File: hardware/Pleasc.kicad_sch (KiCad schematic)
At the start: 96 parts, among them J1 2601-1104, J3 ESQ-110-14-G-D, J4 2601-1104, J5 XT30PW-M, Q1 AO3400A, Q10 AO3400A, Q11 AO3400A, Q12 AO3400A, Q13 AO3400A, Q14 AO3400A, Q2 AO3400A, Q3 AO3400A, Q4 AO3400A, Q5 AO3400A, Q6 AO3400A, Q7 AO3400A, Q8 AO3400A, Q9 AO3400A, U1 STM32F072C8Tx, U10 LTV-817, U11 LTV-817, U12 LTV-817, U13 LTV-817, U18 LTV-817, U2 TLV70433DBVT, U3 LTV-817, U4 TJA1051T-3, U7 LTV-817, U8 LTV-817, U9 LTV-817

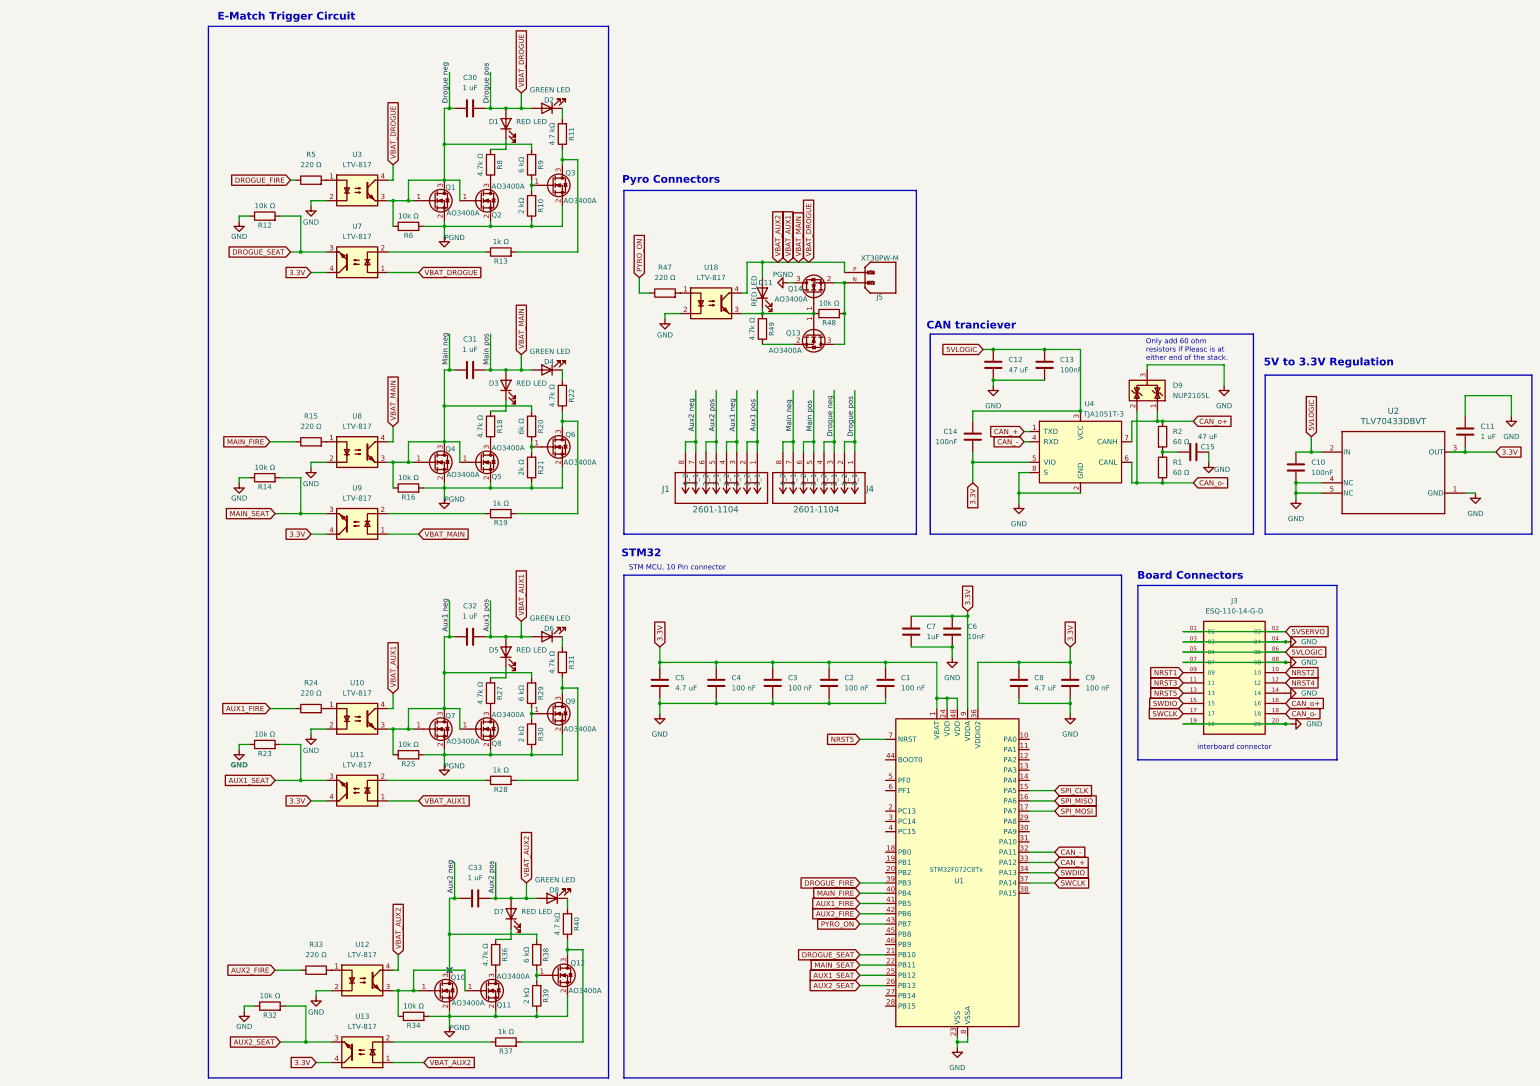
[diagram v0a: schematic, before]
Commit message: Schematic complete, components layed out on the PCB
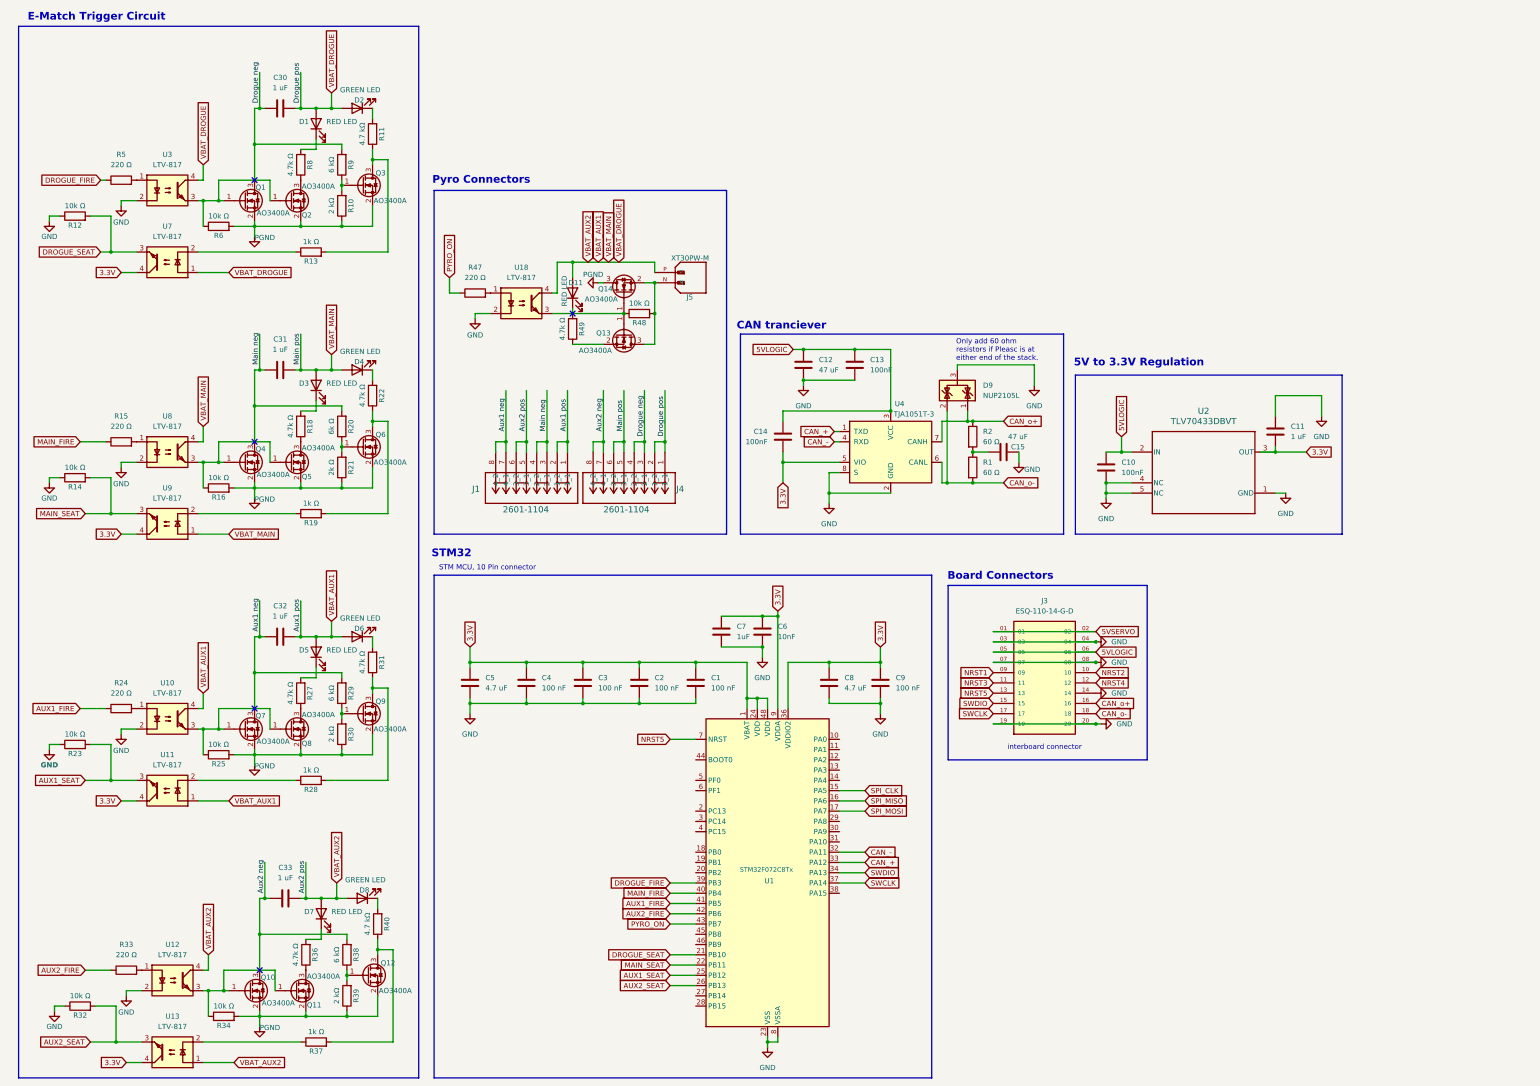
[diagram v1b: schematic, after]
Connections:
- net Aux1 neg: now also J1.7 (4_1), J1.8 (4_2); no longer J1.3 (2_1), J1.4 (2_2), Q7.1 (G), Q8.1 (G), R25.1, U10.3
- net Aux2 neg: now also J4.7 (4_1), J4.8 (4_2); no longer J1.7 (4_1), J1.8 (4_2), Q10.1 (G), Q11.1 (G), R34.1, U12.3
- net Drogue neg: no longer Q1.1 (G), Q2.1 (G), R6.1, U3.3
- net Main neg: now also J1.3 (2_1), J1.4 (2_2); no longer J4.7 (4_1), J4.8 (4_2), Q4.1 (G), Q5.1 (G), R16.1, U8.3
- net at Q13.1 (G), Q14.1 (G), R48.1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: no longer D11.1 (K), R49.2
- new net: Q10.1 (G), Q11.1 (G), R34.1, U12.3
- new net: Q1.1 (G), Q2.1 (G), R6.1, U3.3
- new net: Q4.1 (G), Q5.1 (G), R16.1, U8.3
- new net: D11.1 (K), R49.2
- new net: Q7.1 (G), Q8.1 (G), R25.1, U10.3
- no-connect marks 1 -> 5
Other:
- moved on the sheet: C1, C10, C11, C12, C13, C14, C15, C2, C3, C30, C31, C32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

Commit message: All 4 Pyros circuits routed
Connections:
- net Aux2 neg: now also J4.3 (2_1), J4.4 (2_2); no longer J4.7 (4_1), J4.8 (4_2)
- net Drogue neg: now also J4.7 (4_1), J4.8 (4_2); no longer J4.3 (2_1), J4.4 (2_2)
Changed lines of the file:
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@@
 	)
 	(label "Drogue neg"
-		(at 170.18 121.92 90)
+		(at 160.02 121.92 90)
 		(effects
 			(font
@@
 	)
 	(label "Aux2 neg"
-		(at 160.02 120.65 90)
+		(at 170.18 120.65 90)
 		(effects
 			(font

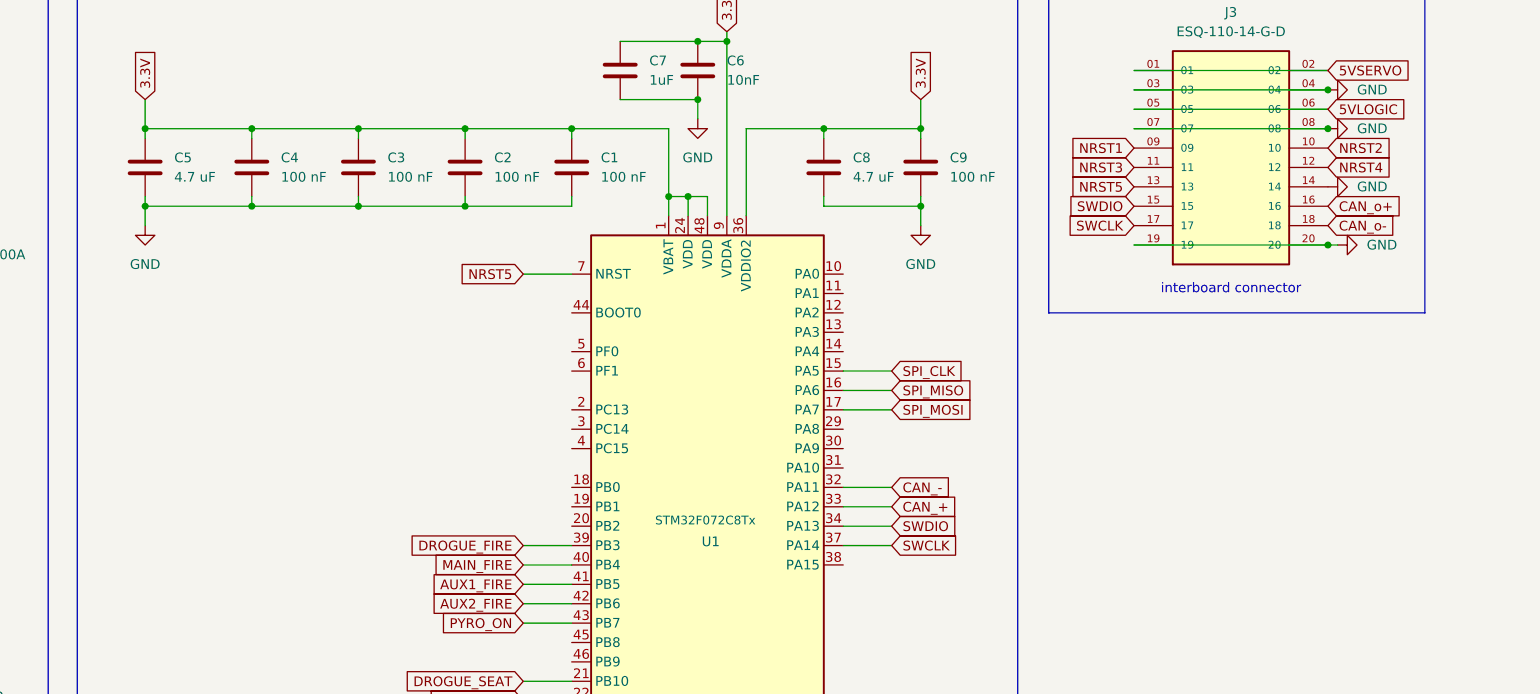
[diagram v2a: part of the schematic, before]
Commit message: added can crystal
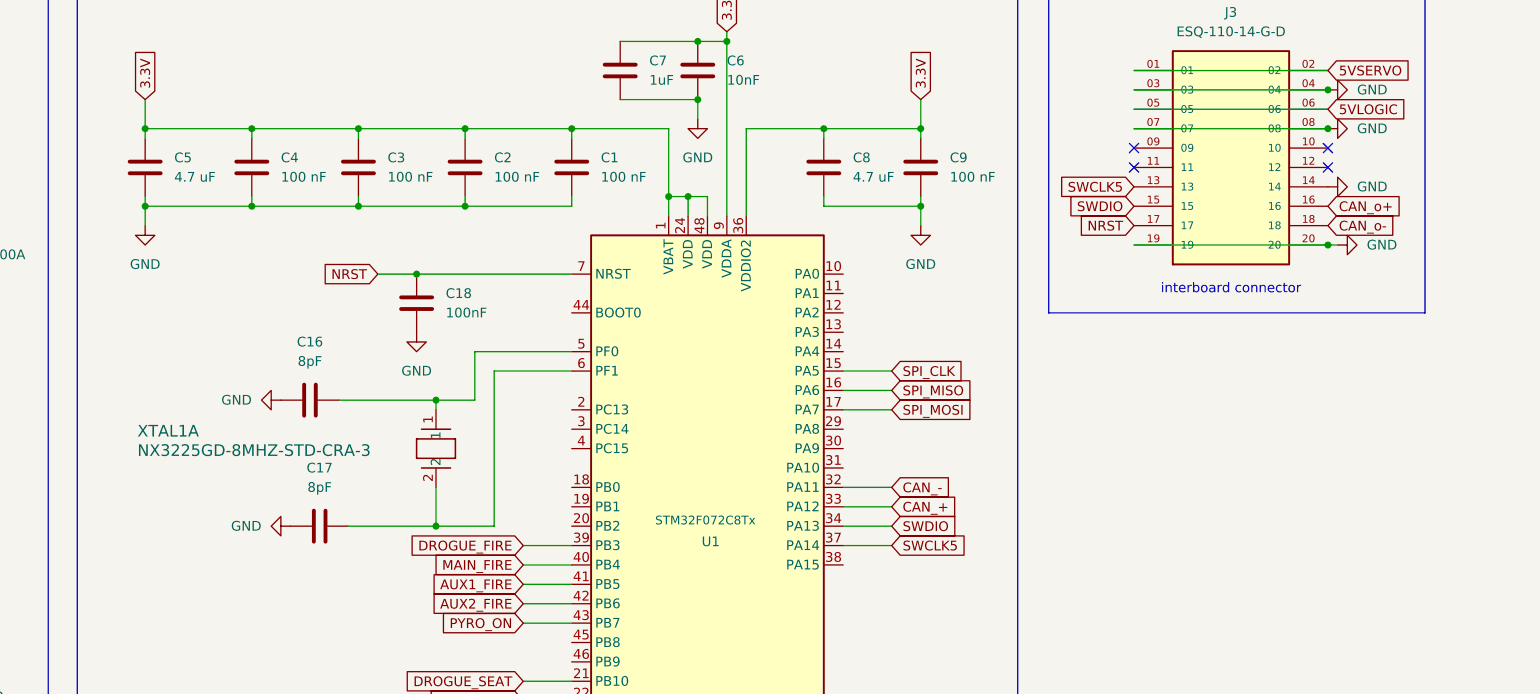
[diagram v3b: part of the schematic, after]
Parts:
- added C16, C17: 8pF, Capacitor_SMD:C_0402_1005Metric, symbol Device:C
- added C18: 100nF, Capacitor_SMD:C_0402_1005Metric, symbol Device:C
- added XTAL1: NX3225GD-8MHZ-STD-CRA-3, XTAL_NX3225GD-8MHZ-STD-CRA-3_NDK, symbol NX3225GD-8MHZ-STD-CRA-3:NX3225GD-8MHZ-STD-CRA-3
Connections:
- net GND: now also C16.1, C17.1, C18.2
- net at U1.5 (PF0): now also C16.2, XTAL1.1
- net at U1.6 (PF1): now also C17.2, XTAL1.2
- net NRST1: no longer names the net of J3.09
- net NRST2: no longer names the net of J3.10
- net NRST3: no longer names the net of J3.11
- net NRST4: no longer names the net of J3.12
- net NRST5 renamed NRST
- net NRST: now also J3.17, C18.1; no longer J3.13
- net SWCLK renamed SWCLK5
- net SWCLK5: now also J3.13; no longer J3.17
- no-connect marks 5 -> 9

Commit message: Version 1.2
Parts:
- removed J5: XT30PW-M, Foinse Footprints:AMASS_XT30PW-M, symbol XT30PW-M:XT30PW-M
- added 3.3V1, CAN-1, GND1, PGND1, PYRO_ON1, VBAT1: S2761-46R, Foinse Footprints:HARWIN_S2761-46R, symbol Test Point:S2761-46R
- added 5V1, CAN+1: S2761, Foinse Footprints:HARWIN_S2761-46R, symbol Test Point:S2761-46R
- added J2: 5023860570, Foinse Footprints:MOLEX_5023860570, symbol Molex Connector:5023860570
- added J5: 39-29-1048, Foinse Footprints:MOLEX_39-29-1048, symbol Molex Battery Connector:39-29-1048
- XTAL1: footprint XTAL_NX3225GD-8MHZ-STD-CRA-3_NDK -> Foinse Footprints:XTAL_NX3225GD-8MHZ-STD-CRA-3_NDK
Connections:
- net 3.3V: now also 3.3V1.1, J2.4
- net 5VLOGIC: now also J3.11, J3.12, 5V1.1; no longer J3.05, J3.06
- net 5VSERVO: now also J3.03, J3.04, J3.05, J3.06, J3.07, J3.08; no longer J3.01, J3.02
- net CAN_o+: now also CAN+1.1
- net CAN_o-: now also CAN-1.1
- net GND: now also J3.01, J3.02, J3.09, J3.10, J3.13, J3.15, J3.17, GND1.1, J2.5, J2.S1 (SHIELD1), J2.S2 (SHIELD2); no longer J3.03, J3.04, J3.07, J3.08
- net NRST: now also J2.3; no longer J3.17
- net PGND: now also PGND1.1
- net PYRO_ON: now also PYRO_ON1.1
- net SWDIO: now also J2.2; no longer J3.15
- net VBAT_AUX1: now also J5.1, J5.2, VBAT1.1
- net at Q13.3 (D), Q14.2 (S), R48.2: now also J5.3, J5.4
- net SWCLK5 renamed SWCLK
- net SWCLK: now also J2.1; no longer J3.13
- no-connect marks 9 -> 5
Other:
- moved on the sheet: C10, C11, C12, C13, C14, C15, C17, D9, R1, R2, U2, U4

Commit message: cleaning
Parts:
- removed C10: 100nF, Capacitor_SMD:C_0402_1005Metric, symbol Device:C
- removed C11: 1 uF, Capacitor_SMD:C_0402_1005Metric, symbol Device:C
- removed U2: TLV70433DBVT, Foinse Footprints:DBV0005A_N, symbol TLV70433DBVT:TLV70433DBVT
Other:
- added sheet power (power.kicad_sch)
- moved on the sheet: 3.3V1, 5V1, GND1

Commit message: ready for review
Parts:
- added R17, R26, R35, R41: 10kΩ, Resistor_SMD:R_0402_1005Metric, symbol Device:R
- R5: value 220 Ω -> 220Ω
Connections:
- net AUX1_FIRE: now also R17.2
- net AUX2_FIRE: now also R41.2
- net DROGUE_FIRE: now also R35.2
- net GND: now also R17.1, R26.1, R35.1, R41.1
- net MAIN_FIRE: now also R26.2

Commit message: ready 2 order
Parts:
- renumbered C30 to C1, C18 to C10, C2 to C11, C1 to C12, C7 to C13, C6 to C14, C8 to C15, C14 to C16, C12 to C17, C9 to C18, C13 to C19, C31 to C2, C15 to C20, C32 to C3, C33 to C4, C4 to C6, C16 to C7, C17 to C8, C3 to C9, D9 to D10, D3 to D2, D5 to D3, D7 to D4, D2 to D5, D4 to D6, D6 to D7, D11 to D9, J2 to J1, J1 to J2, J4 to J3, J5 to J4, J3 to J6, Q6 to Q10, Q9 to Q11, Q14 to Q13, Q13 to Q14, Q4 to Q2, Q7 to Q3, Q10 to Q4, Q2 to Q5, Q5 to Q6, Q8 to Q7, Q11 to Q8, Q3 to Q9, R12 to R1, R15 to R10, R24 to R11, R33 to R12, R6 to R13, R16 to R14, R25 to R15, R34 to R16, R8 to R17, R27 to R19, R14 to R2, R36 to R20, R13 to R21, R19 to R22, R28 to R23, R37 to R24, R9 to R25, R10 to R26, R20 to R27, R21 to R28, R23 to R3, R38 to R31, R39 to R32, R11 to R33, R22 to R34, R31 to R35, R40 to R36, R47 to R37, R49 to R38, R48 to R39, R32 to R4, R2 to R40, R1 to R41, R26 to R5, R17 to R6, R41 to R7, R35 to R8, R5 to R9, U3 to U1, U1 to U10, U4 to U11, U7 to U2, U8 to U3, U9 to U4, U10 to U5, U11 to U6, U12 to U7, U13 to U8, U18 to U9

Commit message: hardware done
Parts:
- C14, C17, C20: footprint Capacitor_SMD:C_0402_1005Metric -> Capacitor_SMD:C_0603_1608Metric
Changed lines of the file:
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@@
 			)
 		)
-		(property "Footprint" "Capacitor_SMD:C_0402_1005Metric"
+		(property "Footprint" "Capacitor_SMD:C_0603_1608Metric"
 			(at 275.59 126.6952 0)
 			(effects
@@
 			)
 		)
-		(property "Footprint" "Capacitor_SMD:C_0402_1005Metric"
+		(property "Footprint" "Capacitor_SMD:C_0603_1608Metric"
 			(at 198.4248 173.99 0)
 			(effects
@@
 			)
 		)
-		(property "Footprint" "Capacitor_SMD:C_0402_1005Metric"
+		(property "Footprint" "Capacitor_SMD:C_0603_1608Metric"
 			(at 223.2152 107.95 0)
 			(effects
